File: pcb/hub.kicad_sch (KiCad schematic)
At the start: 21 parts, among them U3 USB2514B, Y2 24MHz

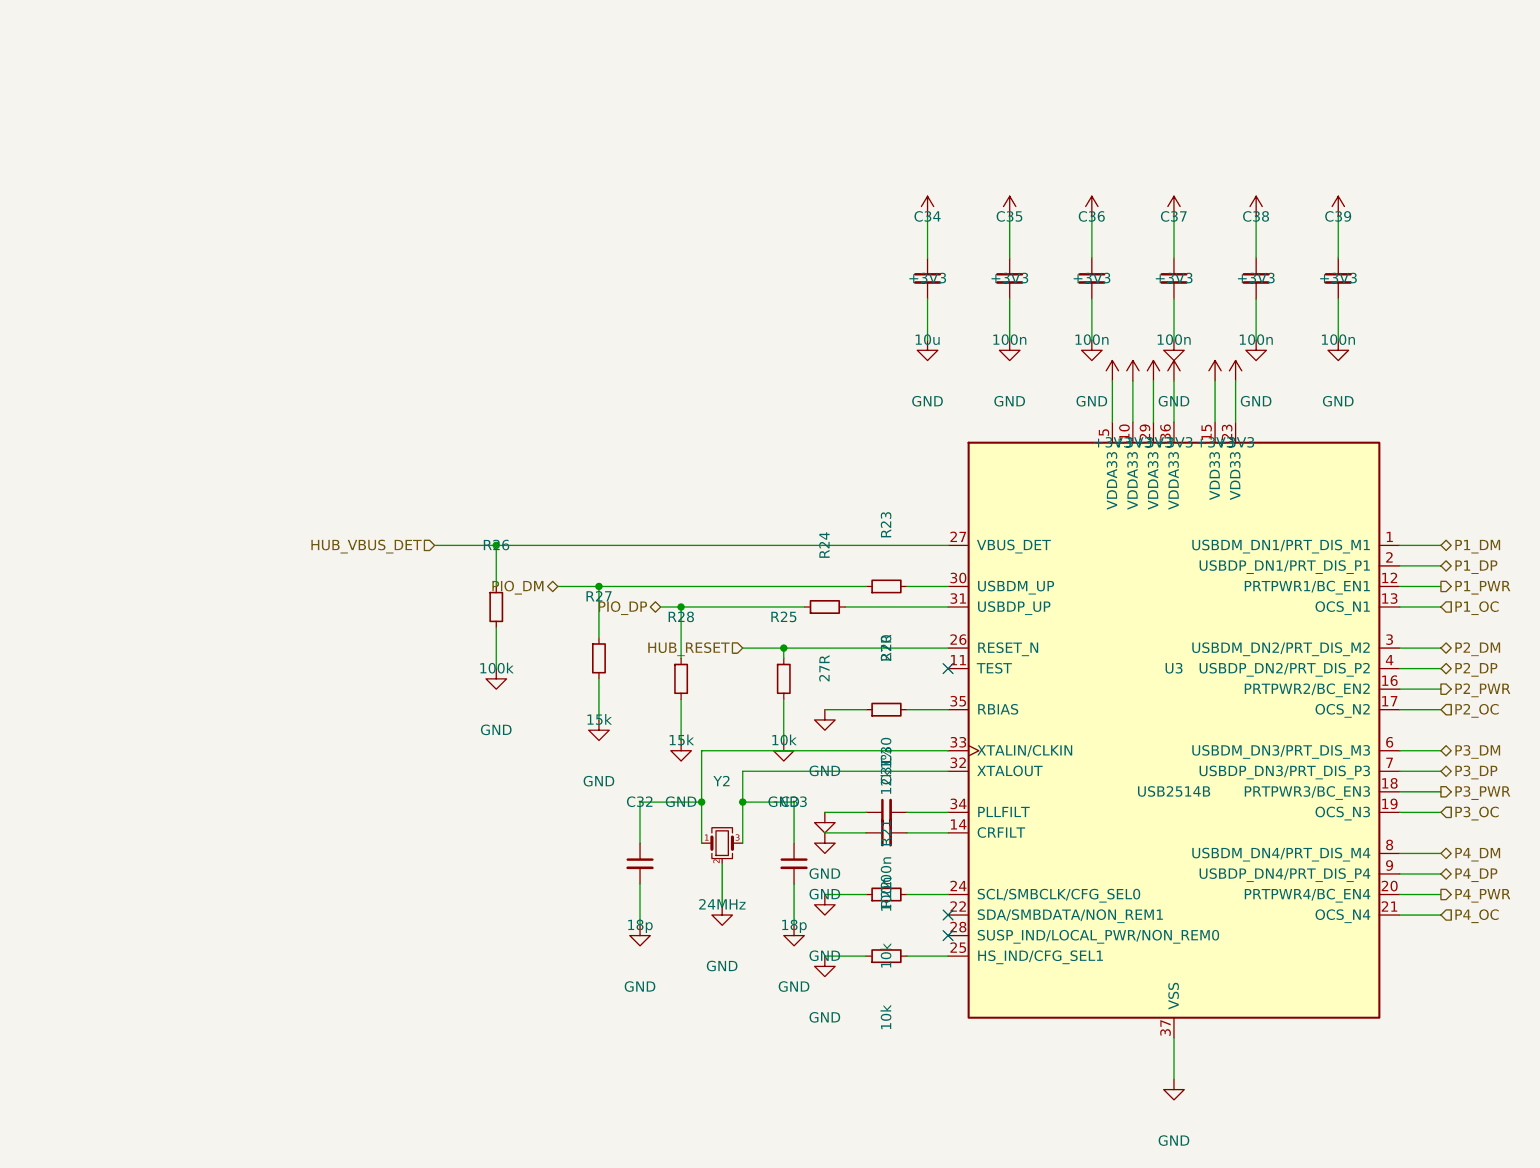
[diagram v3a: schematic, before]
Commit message: draw the port, once, and place it four times
The current-limited switch, the ESD array, the receptacle and the bulk
capacitance. Left to right: the hub's enable arrives, the switch passes 5 V
through, the array protects the pair on its way out, and the receptacle is the
board edge. The fault goes straight back to the hub, which pulls it up itself.

The rails are drawn rather than scattered. Giving every ground pin its own
symbol is quick to generate and tiresome to read -- the sheet fills with
identical glyphs and the shape of the supply disappears -- so the generator now
draws one line, one symbol and a drop to each pin. Same netlist, a tenth of the
symbols. That is the change that was asked for after the same tidying had been
done by hand twice.

Three bugs had to be found on the way, and the first two hid the third.

A symbol may be mirrored, because a connector drawn with its pins facing out of
the package has them facing the wrong way at the right-hand edge of a sheet, and
turning it over instead would reverse the pin order that the pair has to line up
with. The mirror flag was first built as a string of escape sequences and passed
through a plain substitution, which does not interpret them: the literal
characters went into the file, the symbol was malformed, and KiCad stopped
reading the sheet at that point. What it reported was that the sheet had no
hierarchical labels -- which was true, in the sense that it had never got to
them.

The per-placement references then leaked into the reference field itself, which
belongs to one reference; the list belongs only in the instance paths.

And the placements were being read in file order, which the editor is free to
change when it saves -- it had already put them in the order 4, 3, 1, 2. The
references now follow the sheet names, and the generator refuses to run if it
does not find exactly four.

Co-Authored-By: Claude Opus 5 (1M context) <noreply@anthropic.com>
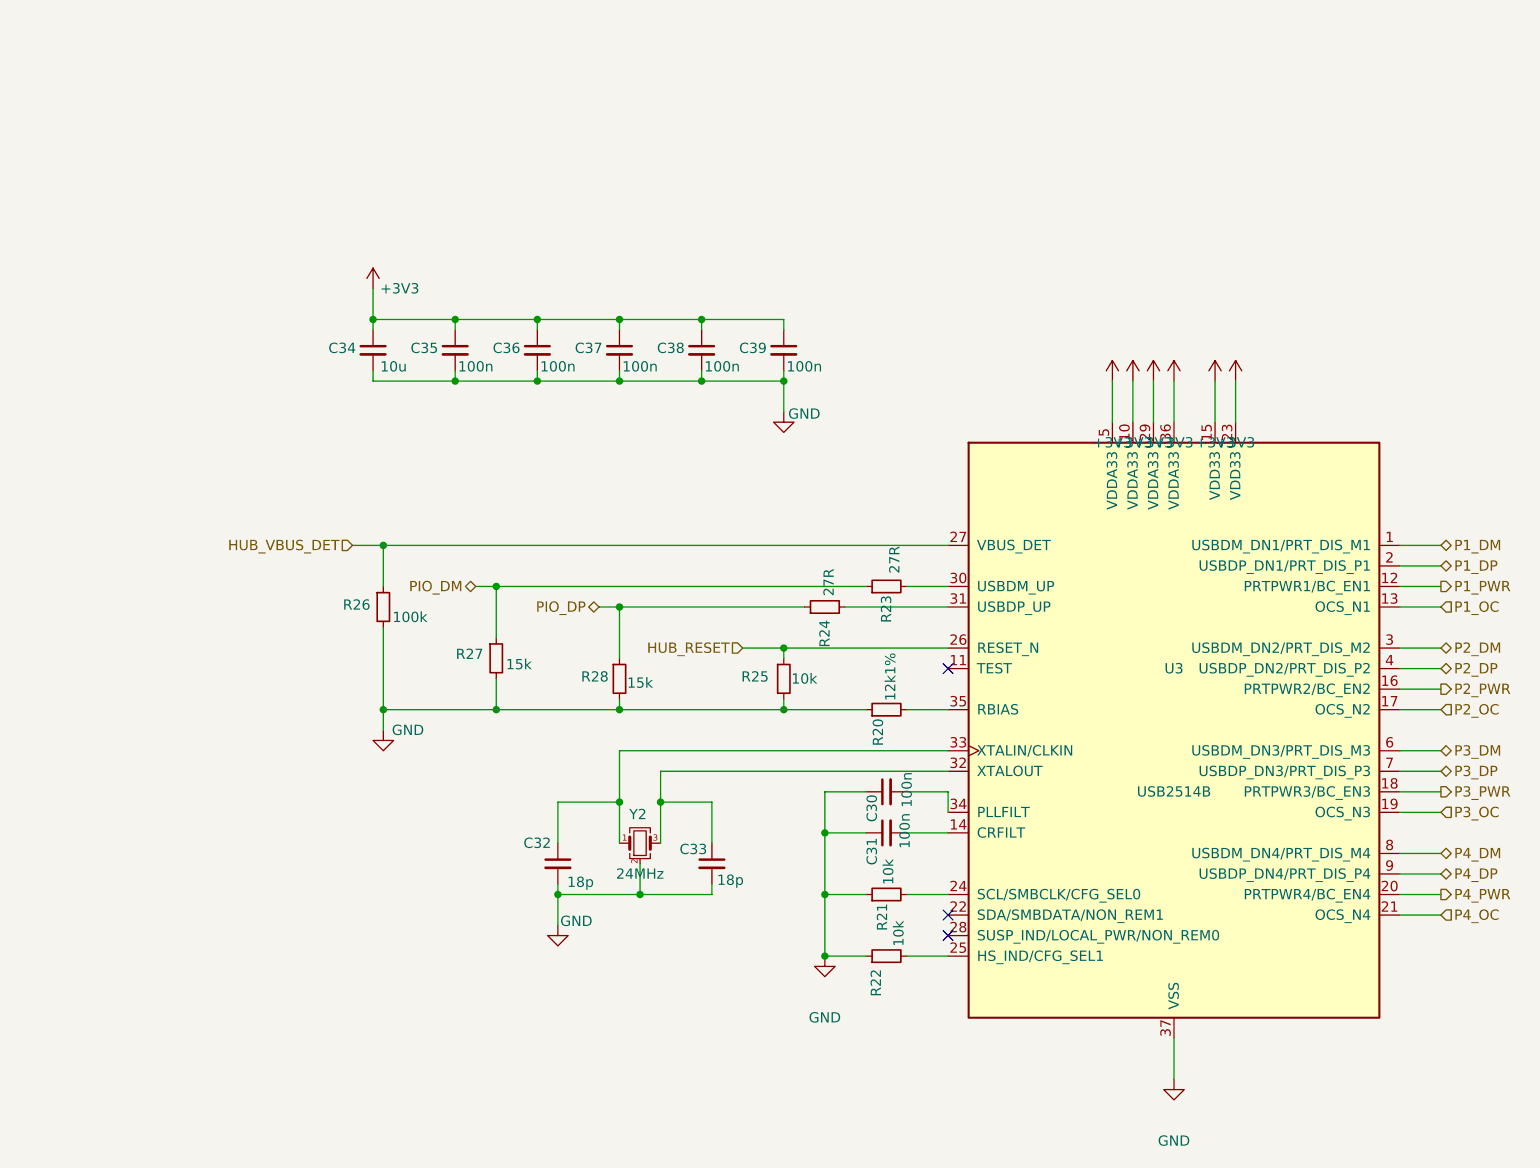
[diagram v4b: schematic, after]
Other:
- moved on the sheet: C30, C32, C33, C34, C35, C36, C37, C38, C39, R26, R27, R28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

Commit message: specify every capacitor: a rating and a dielectric, chosen from its net
A value on its own is not a specification. Each of the 62 capacitor symbols now carries a voltage
rating and a dielectric picked from the net it sits on -- at least twice the working voltage,
rounded to a standard rating, and never below what a socket the user can reach can present. Both
are hidden fields, so the drawing stays readable and a bill of materials can still be made from it.

Two of the choices are decisions rather than arithmetic.

The connector-side parts are rated for abuse at 50V, because nothing on the board protects them:
both input switches sit downstream of them, so the sink's own supply decoupling and the data
port's see whatever a hostile charger produces with no switch in between.

The charger's input bank is rated 25V on a condition, and the condition is firmware. The input
over-voltage trip defaults to 26V, which is above a 25V part, so rating the bank for its working
voltage is only safe if that trip comes down. The part offers 7V, 12V, 22V and 26V and 12V is the
right one here: the sink never asks for more than 9V, so 12V clears the profile with room and
bounds what the bank can ever see. A board decision that creates a firmware requirement is exactly
the sort that gets lost, so it is recorded on both sides.

What is left open is what the banks are worth once fitted. The charger specifies them as counts of
10uF parts, which only means something if each part is still worth 10uF where it sits, and a
ceramic at 9V is not. The rating and the dielectric are settled; the package is not, and the
package is what decides how much survives. The footprint step has to read each chosen part's bias
curve and add parts if the effective value falls short rather than assume the count was the point.
That is the one piece of this specification that can still change the part count.

Rules check unchanged, and the schematic check is clean.

Co-Authored-By: Claude Opus 5 (1M context) <norepl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
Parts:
- C30, C31, C34, C35, C36, C37, C38, C39: Dielectric (none) -> X7R; Voltage (none) -> 16V
- C32, C33: Dielectric (none) -> C0G; Voltage (none) -> 50V
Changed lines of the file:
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@@
+			)
+		)
+		(property "Voltage" "50V"
+			(at 148.336 145.542 0)
+			(show_name no)
+			(do_not_autoplace no)
+			(effects
+				(font
+					(size 1.27 1.27)
+				)
+				(hide yes)
+			)
+		)
+		(property "Dielectric" "C0G"
+			(at 148.336 145.542 0)
+			(show_name no)
+			(do_not_autoplace no)
+			(effects
+				(font
+					(size 1.27 1.27)
+				)
+				(hide yes)
 			)
 		)
@@
 			)
 		)
+		(property "Voltage" "16V"
+			(at 169.926 139.446 0)
+			(show_name no)
+			(do_not_autoplace no)
+			(effects
+				(font
+					(size 1.27 1.27)
+				)
+				(hide yes)
+			)
+		)
+		(property "Dielectric" "X7R"
+			(at 169.926 139.446 0)
+			(show_name no)
+			(do_not_autoplace no)
+			(effects
+				(font
+					(size 1.27 1.27)
+				)
+				(hide yes)
+			)
+		)
 		(property "Footprint" ""
 			(at 167.64 139.7 0)
@@
 					(size 1.27 1.27)
 				)
+			)
+		)
+		(property "Voltage" "16V"
+			(at 116.84 82.042 0)
+			(show_name no)
+			(do_not_autoplace no)
+			(effects
+				(font
+					(size 1.27 1.27)
+				)
+				(hide yes)
+			)
+		)
+		(property "Dielectric" "X7R"
+			(at 116.84 82.042 0)
+			(show_name no)
+			(do_not_autoplace no)
+			(effects
+				(font
+					(size 1.27 1.27)
+				)
+				(hide yes)
 			)
 		)
@@
 			)
 		)
+		(property "Voltage" "16V"
+			(at 170.18 134.366 0)
+			(show_name no)
+			(do_not_autoplace no)
+			(effects
+				(font
+					(size 1.27 1.27)
+				)
+				(hide yes)
+			)
+		)
+		(property "Dielectric" "X7R"
+			(at 170.18 134.366 0)
+			(show_name no)
+			(do_not_autoplace no)
+			(effects
+				(font
+					(size 1.27 1.27)
+				)
+				(hide yes)
+			)
+		)
 		(property "Footprint" ""
 			(at 167.64 134.62 0)
@@
 					(size 1.27 1.27)
 				)
+			)
+		)
+		(property "Voltage" "16V"
+			(at 106.68 82.042 0)
+			(show_name no)
+			(do_not_autoplace no)
+			(effects
+				(font
+					(size 1.27 1.27)
+				)
+				(hide yes)
+			)
+		)
+		(property "Dielectric" "X7R"
+			(at 106.68 82.042 0)
+			(show_name no)
+			(do_not_autoplace no)
+			(effects
+				(font
+					(size 1.27 1.27)
+				)
+				(hide yes)
 			)
 		)
@@
 			)
 		)
+		(property "Voltage" "50V"
+			(at 129.794 145.796 0)
+			(show_name no)
+			(do_not_autoplace no)
+			(effects
+				(font
+					(size 1.27 1.27)
+				)
+				(hide yes)
+			)
+		)
+		(property "Dielectric" "C0G"
+			(at 129.794 145.796 0)
+			(show_name no)
+			(do_not_autoplace no)
+			(effects
+				(font
+					(size 1.27 1.27)
+				)
+				(hide yes)
+			)
+		)
 		(property "Footprint" ""
 			(at 127 143.51 0)
@@
 			)
 		)
+		(property "Voltage" "16V"
+			(at 147.32 82.042 0)
+			(show_name no)
+			(do_not_autoplace no)
+			(effects
+				(font
+					(size 1.27 1.27)
+				)
+				(hide yes)
+			)
+		)
+		(property "Dielectric" "X7R"
+			(at 147.32 82.042 0)
+			(show_name no)
+			(do_not_autoplace no)
+			(effects
+				(font
+					(size 1.27 1.27)
+				)
+				(hide yes)
+			)
+		)
 		(property "Footprint" ""
 			(at 144.78 80.01 0)
@@
 			)
 		)
+		(property "Voltage" "16V"
+			(at 127 82.042 0)
+			(show_name no)
+			(do_not_autoplace no)
+			(effects
+				(font
+					(size 1.27 1.27)
+				)
+				(hide yes)
+			)
+		)
+		(property "Dielectric" "X7R"
+			(at 127 82.042 0)
+			(show_name no)
+			(do_not_autoplace no)
+			(effects
+				(font
+					(size 1.27 1.27)
+				)
+				(hide yes)
+			)
+		)
 		(property "Footprint" ""
 			(at 124.46 80.01 0)
@@
 					(size 1.27 1.27)
 				)
+			)
+		)
+		(property "Voltage" "16V"
+			(at 137.16 82.042 0)
+			(show_name no)
+			(do_not_autoplace no)
+			(effects
+				(font
+					(size 1.27 1.27)
+				)
+				(hide yes)
+			)
+		)
+		(property "Dielectric" "X7R"
+			(at 137.16 82.042 0)
+			(show_name no)
+			(do_not_autoplace no)
+			(effects
+				(font
+					(size 1.27 1.27)
+				)
+				(hide yes)
 			)
 		)
@@
 			)
 		)
+		(property "Voltage" "16V"
+			(at 157.48 82.042 0)
+			(show_name no)
+			(do_not_autoplace no)
+			(effects
+				(font
+					(size 1.27 1.27)
+				)
+				(hide yes)
+			)
+		)
+		(property "Dielectric" "X7R"
+			(at 157.48 82.042 0)
+			(show_name no)
+			(do_not_autoplace no)
+			(effects
+				(font
+					(size 1.27 1.27)
+				)
+				(hide yes)
+			)
+		)

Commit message: specify the resistors, and round three values that were never parts
Every resistor now carries a tolerance, and it is 1% only where the value is read: a reference a
part trims itself against, a divider ratio, a termination that states what this end of a cable is,
a value that programs a threshold at power-on. Nineteen of the thirty-eight qualify; the rest are
pull-ups, pull-downs, straps and series parts, where 5% is honest and 1% buys nothing. Power is not
a field, because the largest dissipation anywhere on the board is a few milliwatts in an
indicator's series resistor.

Three values were arithmetic nobody had rounded. 5.24k and 30.31k are the charger vendor's own
calculated figures for the temperature network and neither exists as a part; 172k was ours for the
boost's current limit and is not a standard value either. They become 5.23k, 30.1k and 174k, and
what each costs is recorded: a fraction of a degree on the temperature thresholds, about 2% on the
current limit. A fourth, the hub's reference resistor, had its tolerance written into the value
string; that moves to the field where it belongs.

Reading the boost's datasheet to round the current limit corrected how it had been described. The
limit is not set at the worst-case peak -- the switch has to pass about 4.25A at the bottom of the
cell with every port loaded, so a limit there would trip in normal service. It sits at about 5.9A,
clearing that peak by nearly 40%. The vendor publishes two resistances against measured limits,
which fixes both the relationship and its direction: more resistance, less current.

Rules check unchanged, schematic check clean.

Co-Authored-By: Claude Opus 5 (1M context) <noreply@anthropic.com>
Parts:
- R20: value 12k1% -> 12k; Tolerance (none) -> 1%
- R21, R22, R25, R26, R27, R28: Tolerance (none) -> 5%
- R23, R24: Tolerance (none) -> 1%
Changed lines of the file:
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@@
+			)
+		)
+		(property "Tolerance" "5%"
+			(at 167.894 144.526 0)
+			(show_name no)
+			(do_not_autoplace no)
+			(effects
+				(font
+					(size 1.27 1.27)
+				)
+				(hide yes)
 			)
 		)
@@
 			)
 		)
+		(property "Tolerance" "5%"
+			(at 108.712 113.03 0)
+			(show_name no)
+			(do_not_autoplace no)
+			(effects
+				(font
+					(size 1.27 1.27)
+				)
+				(hide yes)
+			)
+		)
 		(property "Footprint" ""
 			(at 105.41 111.76 0)
@@
 			)
 		)
+		(property "Tolerance" "1%"
+			(at 168.656 105.918 0)
+			(show_name no)
+			(do_not_autoplace no)
+			(effects
+				(font
+					(size 1.27 1.27)
+				)
+				(hide yes)
+			)
+		)
 		(property "Footprint" ""
 			(at 167.64 109.22 0)
@@
 			)
 		)
+		(property "Tolerance" "5%"
+			(at 169.164 152.146 0)
+			(show_name no)
+			(do_not_autoplace no)
+			(effects
+				(font
+					(size 1.27 1.27)
+				)
+				(hide yes)
+			)
+		)
 		(property "Footprint" ""
 			(at 167.64 154.94 0)
@@
 					(size 1.27 1.27)
 				)
+			)
+		)
+		(property "Tolerance" "5%"
+			(at 122.174 118.872 0)
+			(show_name no)
+			(do_not_autoplace no)
+			(effects
+				(font
+					(size 1.27 1.27)
+				)
+				(hide yes)
 			)
 		)
@@
 			)
 		)
+		(property "Tolerance" "1%"
+			(at 160.528 108.712 0)
+			(show_name no)
+			(do_not_autoplace no)
+			(effects
+				(font
+					(size 1.27 1.27)
+				)
+				(hide yes)
+			)
+		)
 		(property "Footprint" ""
 			(at 160.02 111.76 0)
@@
 			)
 		)
-		(property "Value" "12k1%"
+		(property "Value" "12k"
 			(at 168.148 120.396 0)
 			(show_name no)
@@
 					(size 1.27 1.27)
 				)
+			)
+		)
+		(property "Tolerance" "1%"
+			(at 168.148 120.396 0)
+			(show_name no)
+			(do_not_autoplace no)
+			(effects
+				(font
+					(size 1.27 1.27)
+				)
+				(hide yes)
 			)
 		)
@@
 			)
 		)
+		(property "Tolerance" "5%"
+			(at 157.48 120.65 0)
+			(show_name no)
+			(do_not_autoplace no)
+			(effects
+				(font
+					(size 1.27 1.27)
+				)
+				(hide yes)
+			)
+		)
 		(property "Footprint" ""
 			(at 154.94 120.65 0)
@@
 			)
 		)
+		(property "Tolerance" "5%"
+			(at 137.16 121.158 0)
+			(show_name no)
+			(do_not_autoplace no)
+			(effects
+				(font
+					(size 1.27 1.27)
+				)
+				(hide yes)
+			)
+		)

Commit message: specify the magnetics and the crystals by what they have to do
Each inductor now states the current it has to stay unsaturated to, derived rather than copied: the
processor's own datasheet fixes 1.5A for the core regulator, the charger's output side carries
about 6.3A when the input is delivering its full 27W into a system near 4V, and each of the two
converters wants an inductor that holds up past its own current limit so the part protects itself
before the magnetics give up. The crystals state a load capacitance, which is the number that
actually decides whether they oscillate on frequency.

Two things came out of reading rather than assuming.

The charger's inductor value is not a choice. Its datasheet is explicit that 1.5MHz works only with
1uH and 750kHz only with 2.2uH, and the frequency was already fixed at power-on by the resistor
that also sets the cell count. That resistor therefore picks the inductor, and the two have to move
together or not at all. They are consistent as drawn; the coupling is now written down so they stay
that way.

The core regulator's inductor has to be fully shielded and marked for polarity, and oriented as the
vendor's layout shows, because stray field from it couples into the regulator's control loop and
moves the output even with nominally shielded parts. That is a placement constraint arriving from a
component datasheet, and it is recorded where layout will look for it rather than left in a PDF.

The processor's crystal wants a 10pF load, which the 15pF pair either side of it meets once a
couple of picofarads of stray are allowed. The hub's pair implies about 12pF by the same
arithmetic, and that one stays open: its datasheet and design checklist are both scanned images,
so nothing reads out of them without rendering the pages.

Co-Authored-By: Claude Opus 5 (1M context) <noreply@anthropic.com>
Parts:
- Y2: Load (none) -> 12pF; Tolerance (none) -> 30ppm
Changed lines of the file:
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@@
+			)
+		)
+		(property "Tolerance" "30ppm"
+			(at 137.16 144.78 0)
+			(show_name no)
+			(do_not_autoplace no)
+			(effects
+				(font
+					(size 1.27 1.27)
+				)
+				(hide yes)
+			)
+		)
+		(property "Load" "12pF"
+			(at 137.16 144.78 0)
+			(show_name no)
+			(do_not_autoplace no)
+			(effects
+				(font
+					(size 1.27 1.27)
+				)
+				(hide yes)
 			)
 		)
